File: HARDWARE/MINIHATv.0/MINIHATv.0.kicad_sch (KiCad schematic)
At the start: 0 parts

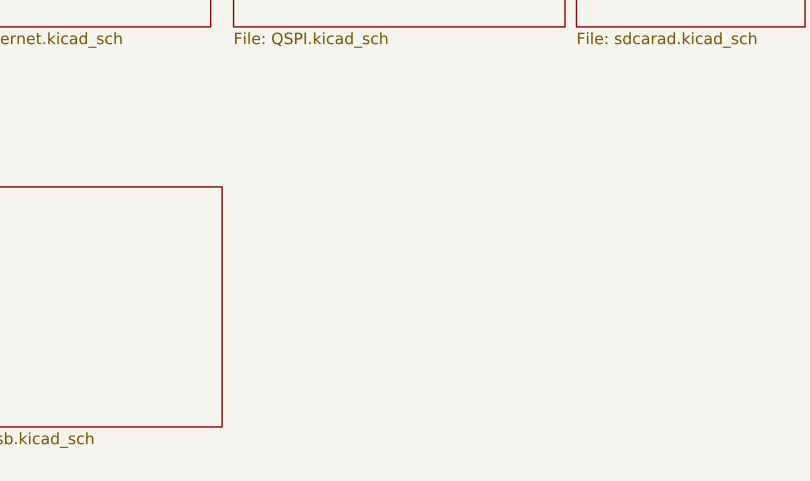
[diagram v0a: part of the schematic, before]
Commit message: added sdram schematic
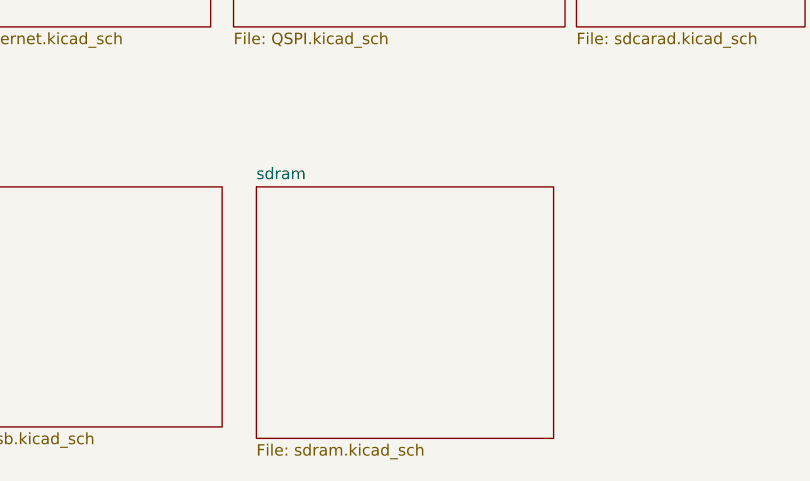
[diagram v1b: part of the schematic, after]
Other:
- added sheet sdram (sdram.kicad_sch)
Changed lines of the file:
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@@
+	)
+	(sheet
+		(at 132.08 130.81)
+		(size 33.02 27.94)
+		(exclude_from_sim no)
+		(in_bom yes)
+		(on_board yes)
+		(dnp no)
+		(fields_autoplaced yes)
+		(stroke
+			(width 0.1524)
+			(type solid)
+		)
+		(fill
+			(color 0 0 0 0)
+		)
+		(property "Sheetname" "sdram"
+			(at 132.08 130.0984 0)
+			(show_name no)
+			(do_not_autoplace no)
+			(effects
+				(font
+					(size 1.27 1.27)
+				)
+				(justify left bottom)
+			)
+		)
+		(property "Sheetfile" "sdram.kicad_sch"
+			(at 132.08 159.3346 0)
+			(show_name no)
+			(do_not_autoplace no)
+			(effects
+				(font
+					(size 1.27 1.27)
+				)
+				(justify left top)
+			)
+		)
+		(instances
+			(project "MINIHATv.0"
+				(path "/19041ef4-1d16-4363-8780-721ad9f20b33"
+					(page "7")
+				)
+			)
+		)
 	)
 	(sheet

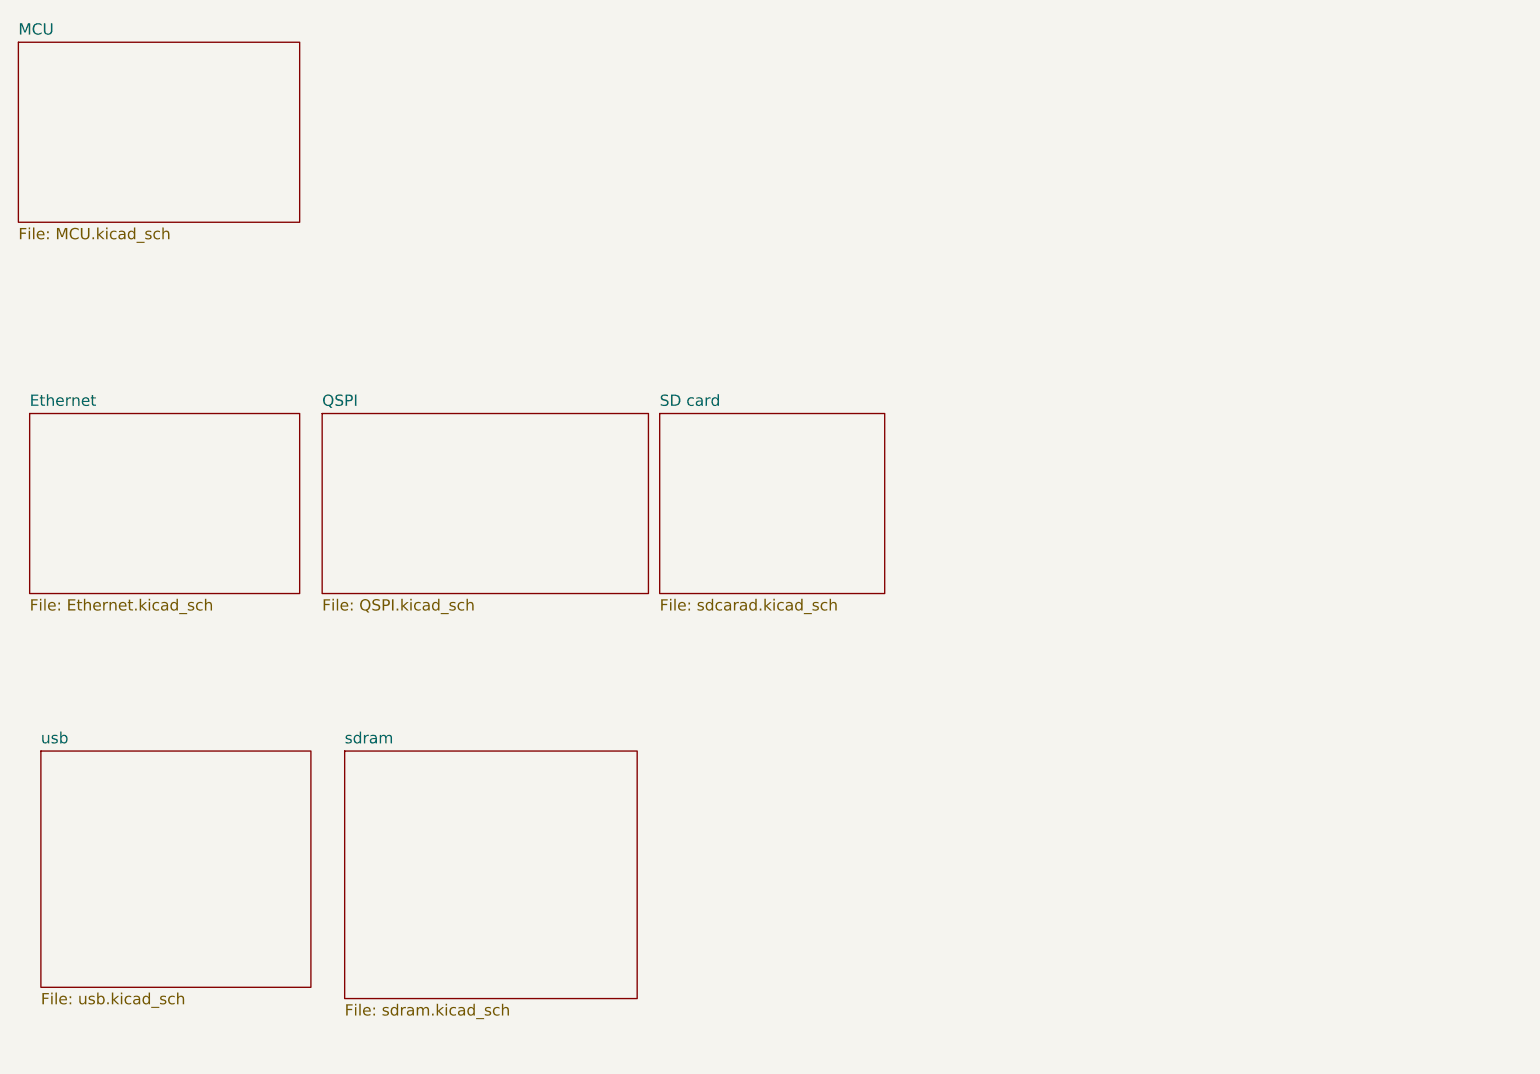
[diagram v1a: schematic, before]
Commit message: added normal buses
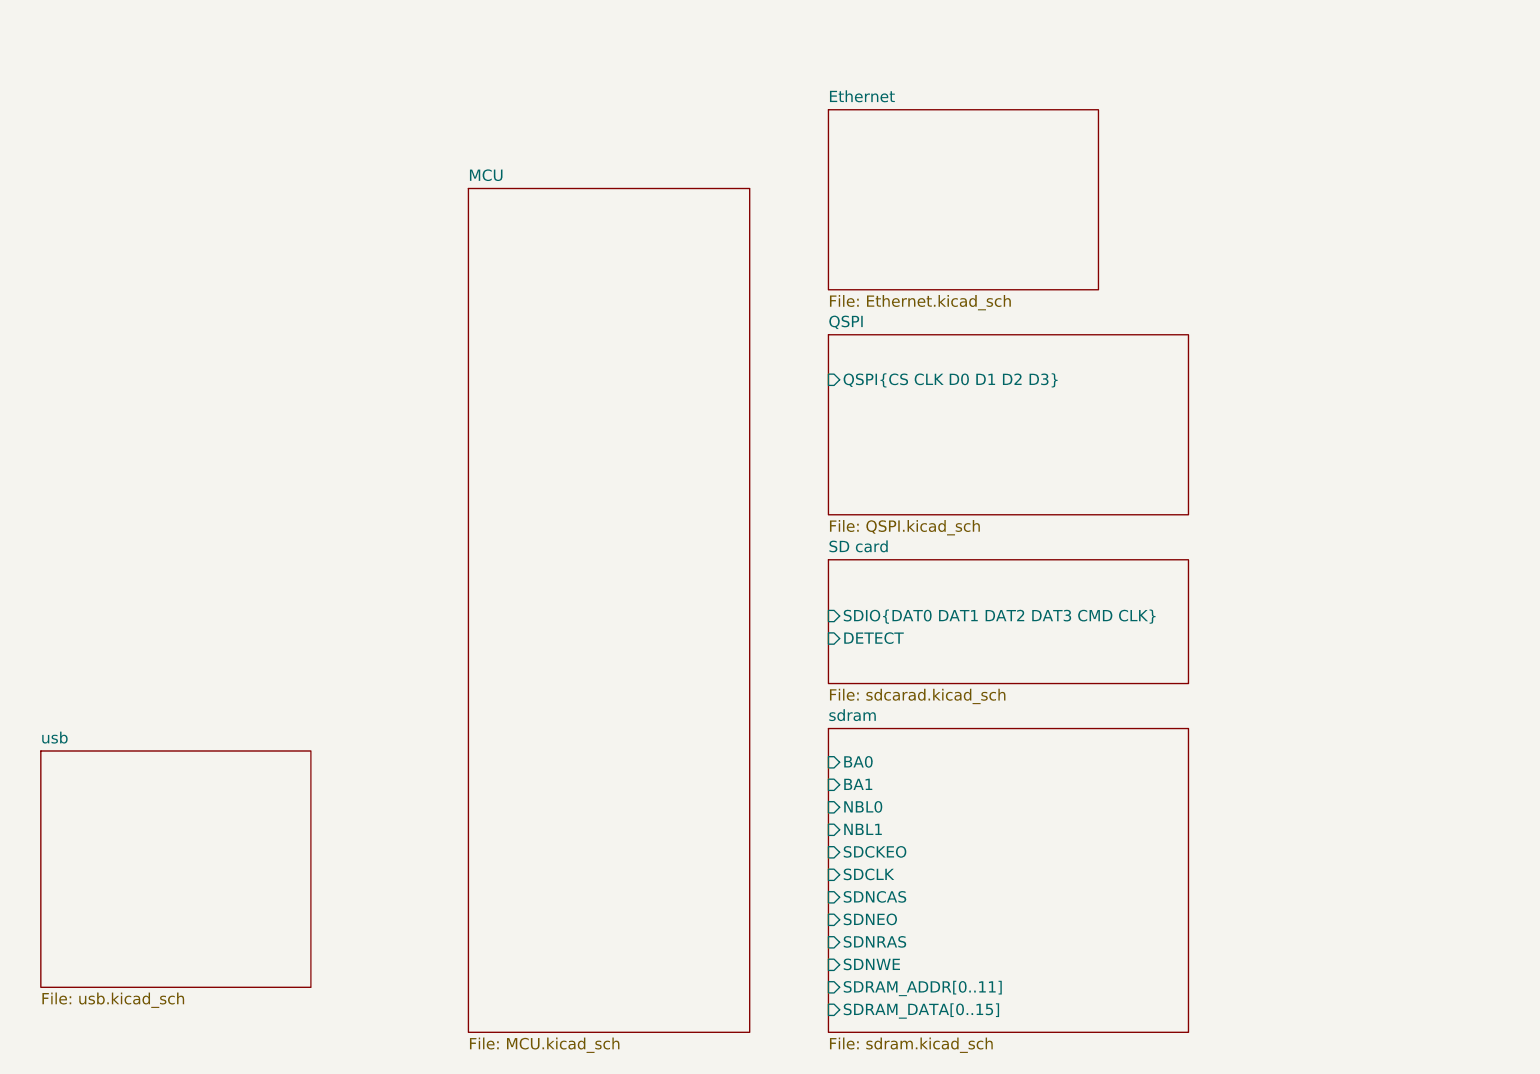
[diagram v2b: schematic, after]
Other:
- sheet QSPI ports: added QSPI{CS CLK D0 D1 D2 D3}; removed none
- sheet SD card ports: added DETECT, SDIO{DAT0 DAT1 DAT2 DAT3 CMD CLK}; removed none
- sheet sdram ports: added BA0, BA1, NBL0, NBL1, SDCKEO, SDCLK, SDNCAS, SDNEO, SDNRAS, SDNWE, SDRAM_ADDR[0..11], SDRAM_DATA[0..15]; removed none
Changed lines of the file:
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@@
 	)
 	(sheet
-		(at 167.64 92.71)
-		(size 25.4 20.32)
+		(at 186.69 109.22)
+		(size 40.64 13.97)
 		(exclude_from_sim no)
 		(in_bom yes)
@@
 		)
 		(property "Sheetname" "SD card"
-			(at 167.64 91.9984 0)
+			(at 186.69 108.5084 0)
 			(show_name no)
 			(do_not_autoplace no)
@@
 		)
 		(property "Sheetfile" "sdcarad.kicad_sch"
-			(at 167.64 113.6146 0)
+			(at 186.69 123.7746 0)
 			(show_name no)
 			(do_not_autoplace no)
@@
 				)
 				(justify left top)
+			)
+		)
+		(pin "DETECT" input
+			(at 186.69 118.11 180)
+			(effects
+				(font
+					(size 1.27 1.27)
+				)
+				(justify left)
+			)
+		)
+		(pin "SDIO{DAT0 DAT1 DAT2 DAT3 CMD CLK}" input
+			(at 186.69 115.57 180)
+			(effects
+				(font
+					(size 1.27 1.27)
+				)
+				(justify left)
 			)
 		)
@@
 	)
 	(sheet
-		(at 132.08 130.81)
-		(size 33.02 27.94)
+		(at 186.69 128.27)
+		(size 40.64 34.29)
 		(exclude_from_sim no)
 		(in_bom yes)
@@
 		)
 		(property "Sheetname" "sdram"
-			(at 132.08 130.0984 0)
+			(at 186.69 127.5584 0)
 			(show_name no)
 			(do_not_autoplace no)
@@
 		)
 		(property "Sheetfile" "sdram.kicad_sch"
-			(at 132.08 159.3346 0)
+			(at 186.69 163.1446 0)
 			(show_name no)
 			(do_not_autoplace no)
@@
 				)
 				(justify left top)
+			)
+		)
+		(pin "BA0" input
+			(at 186.69 132.08 180)
+			(effects
+				(font
+					(size 1.27 1.27)
+				)
+				(justify left)
+			)
+		)
+		(pin "BA1" input
+			(at 186.69 134.62 180)
+			(effects
+				(font
+					(size 1.27 1.27)
+				)
+				(justify left)
+			)
+		)
+		(pin "NBL0" input
+			(at 186.69 137.16 180)
+			(effects
+				(font
+					(size 1.27 1.27)
+				)
+				(justify left)
+			)
+		)
+		(pin "NBL1" input
+			(at 186.69 139.7 180)
+			(effects
+				(font
+					(size 1.27 1.27)
+				)
+				(justify left)
+			)
+		)
+		(pin "SDCKEO" input
+			(at 186.69 142.24 180)
+			(effects
+				(font
+					(size 1.27 1.27)
+				)
+				(justify left)
+			)
+		)
+		(pin "SDCLK" input
+			(at 186.69 144.78 180)
+			(effects
+				(font
+					(size 1.27 1.27)
+				)
+				(justify left)
+			)
+		)
+		(pin "SDNCAS" input
+			(at 186.69 147.32 180)
+			(effects
+				(font
+					(size 1.27 1.27)
+				)
+				(justify left)
+			)
+		)
+		(pin "SDNEO" input
+			(at 186.69 149.86 180)
+			(effects
+				(font
+					(size 1.27 1.27)
+				)
+				(justify left)
+			)
+		)
+		(pin "SDNRAS" input
+			(at 186.69 152.4 180)
+			(effects
+				(font
+					(size 1.27 1.27)
+				)
+				(justify left)
+			)
+		)
+		(pin "SDNWE" input
+			(at 186.69 154.94 180)
+			(effects
+				(font
+					(size 1.27 1.27)
+				)
+				(justify left)
+			)
+		)
+		(pin "SDRAM_ADDR[0..11]" input
+			(at 186.69 157.48 180)
+			(effects
+				(font
+					(size 1.27 1.27)
+				)
+				(justify left)
+			)
+		)
+		(pin "SDRAM_DATA[0..15]" input
+			(at 186.69 160.02 180)
+			(effects
+				(font
+					(size 1.27 1.27)
+				)
+				(justify left)
 			)
 		)
@@
 	)
 	(sheet
-		(at 96.52 92.71)
+		(at 186.69 58.42)
 		(size 30.48 20.32)
 		(exclude_from_sim no)
@@
 		)
 		(property "Sheetname" "Ethernet"
-			(at 96.52 91.9984 0)
+			(at 186.69 57.7084 0)
 			(show_name no)
 			(do_not_autoplace no)
@@
 		)
 		(property "Sheetfile" "Ethernet.kicad_sch"
-			(at 96.52 113.6146 0)
+			(at 186.69 79.3246 0)
 			(show_name no)
 			(do_not_autoplace no)
@@
 	)
 	(sheet
-		(at 129.54 92.71)
-		(size 36.83 20.32)
+		(at 186.69 83.82)
+		(size 40.64 20.32)
 		(exclude_from_sim no)
 		(in_bom yes)
@@
 		)
 		(property "Sheetname" "QSPI"
-			(at 129.54 91.9984 0)
+			(at 186.69 83.1084 0)
 			(show_name no)
 			(do_not_autoplace no)
@@
 		)
 		(property "Sheetfile" "QSPI.kicad_sch"
-			(at 129.54 113.6146 0)
+			(at 186.69 104.7246 0)
 			(show_name no)
 			(do_not_autoplace no)
@@
 				)
 				(justify left top)
+			)
+		)
+		(pin "QSPI{CS CLK D0 D1 D2 D3}" input
+			(at 186.69 88.9 180)
+			(effects
+				(font
+					(size 1.27 1.27)
+				)
+				(justify left)
 			)
 		)
@@
 	)
 	(sheet
-		(at 95.25 50.8)
-		(size 31.75 20.32)
+		(at 146.05 67.31)
+		(size 31.75 95.25)
 		(exclude_from_sim no)
 		(in_bom yes)
@@
 		)
 		(property "Sheetname" "MCU"
-			(at 95.25 50.0884 0)
+			(at 146.05 66.5984 0)
 			(show_name no)
 			(do_not_autoplace no)
@@
 		)
 		(property "Sheetfile" "MCU.kicad_sch"
-			(at 95.25 71.7046 0)
-			(show_name no)
-			(do_not_autoplace no)
+			(at 146.05 163.1446 0)
+			(show_name no)
+			(do_not_autoplace no)

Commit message: added ethernet hierachical ports
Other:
- sheet Ethernet ports: added ETH_RESET, RMII{TXD0 TXD1 TXDEN RXD0 RXD1 RXER CRS_DV MDIO MDC REFCLK}; removed none
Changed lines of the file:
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@@
 	(sheet
 		(at 186.69 58.42)
-		(size 30.48 20.32)
+		(size 69.85 20.32)
 		(exclude_from_sim no)
 		(in_bom yes)
@@
 			)
 		)
+		(pin "RMII{TXD0 TXD1 TXDEN RXD0 RXD1 RXER CRS_DV MDIO MDC REFCLK}" input
+			(at 186.69 64.77 180)
+			(effects
+				(font
+					(size 1.27 1.27)
+				)
+				(justify left)
+			)
+		)
+		(pin "ETH_RESET" input
+			(at 186.69 67.31 180)
+			(effects
+				(font
+					(size 1.27 1.27)
+				)
+				(justify left)
+			)
+		)
